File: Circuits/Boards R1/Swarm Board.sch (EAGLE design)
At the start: 89 parts, among them CON1 ISP(2X3), T1 NPN2N2222, T10 TEFT4300, T13 NPN2N2222, T14 NPN2N2222, T15 NPN2N2222, T16 NPN2N2222, T17 NPN2N2222, T18 NPN2N2222, T2 NPN2N2222, T3 NPN2N2222, T4 TEFT4300, T5 TEFT4300, T6 TEFT4300, T7 TEFT4300, T8 TEFT4300, T9 TEFT4300, U1 ATMEGA324P, U2 MCP73832SOT-23, U3 TB6552FN/FNG

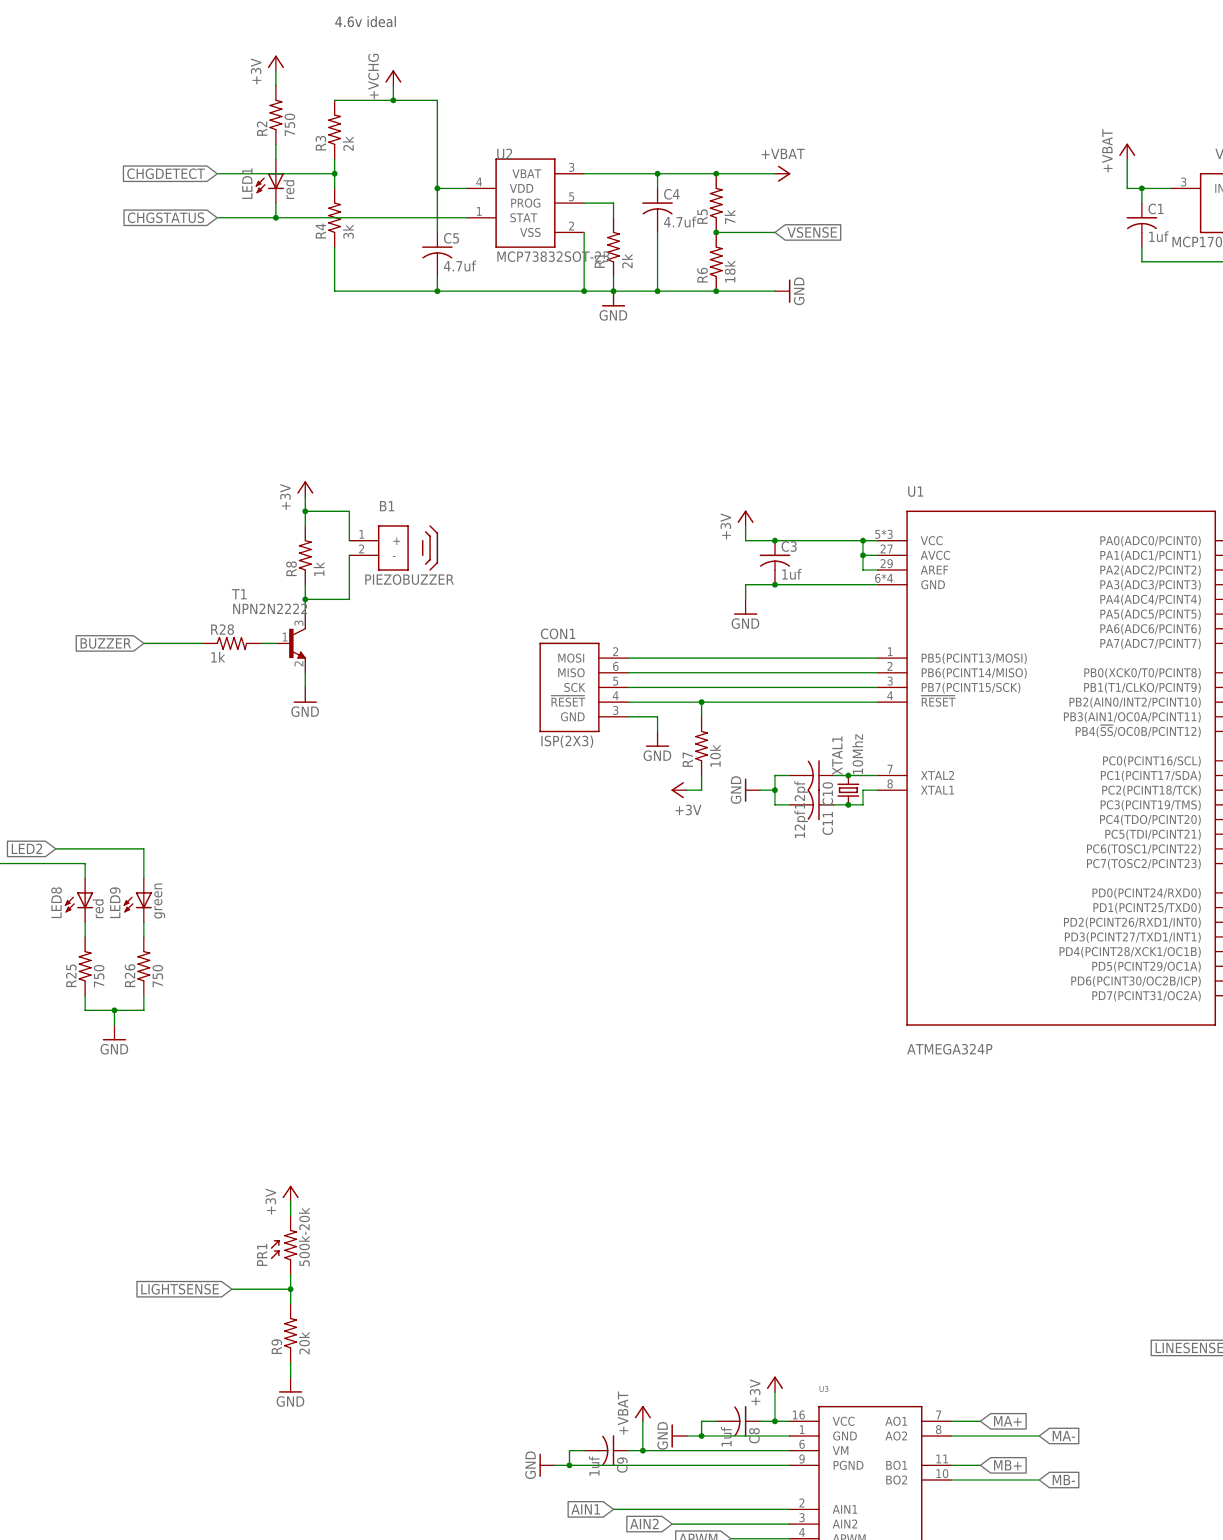
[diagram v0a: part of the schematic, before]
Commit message: 
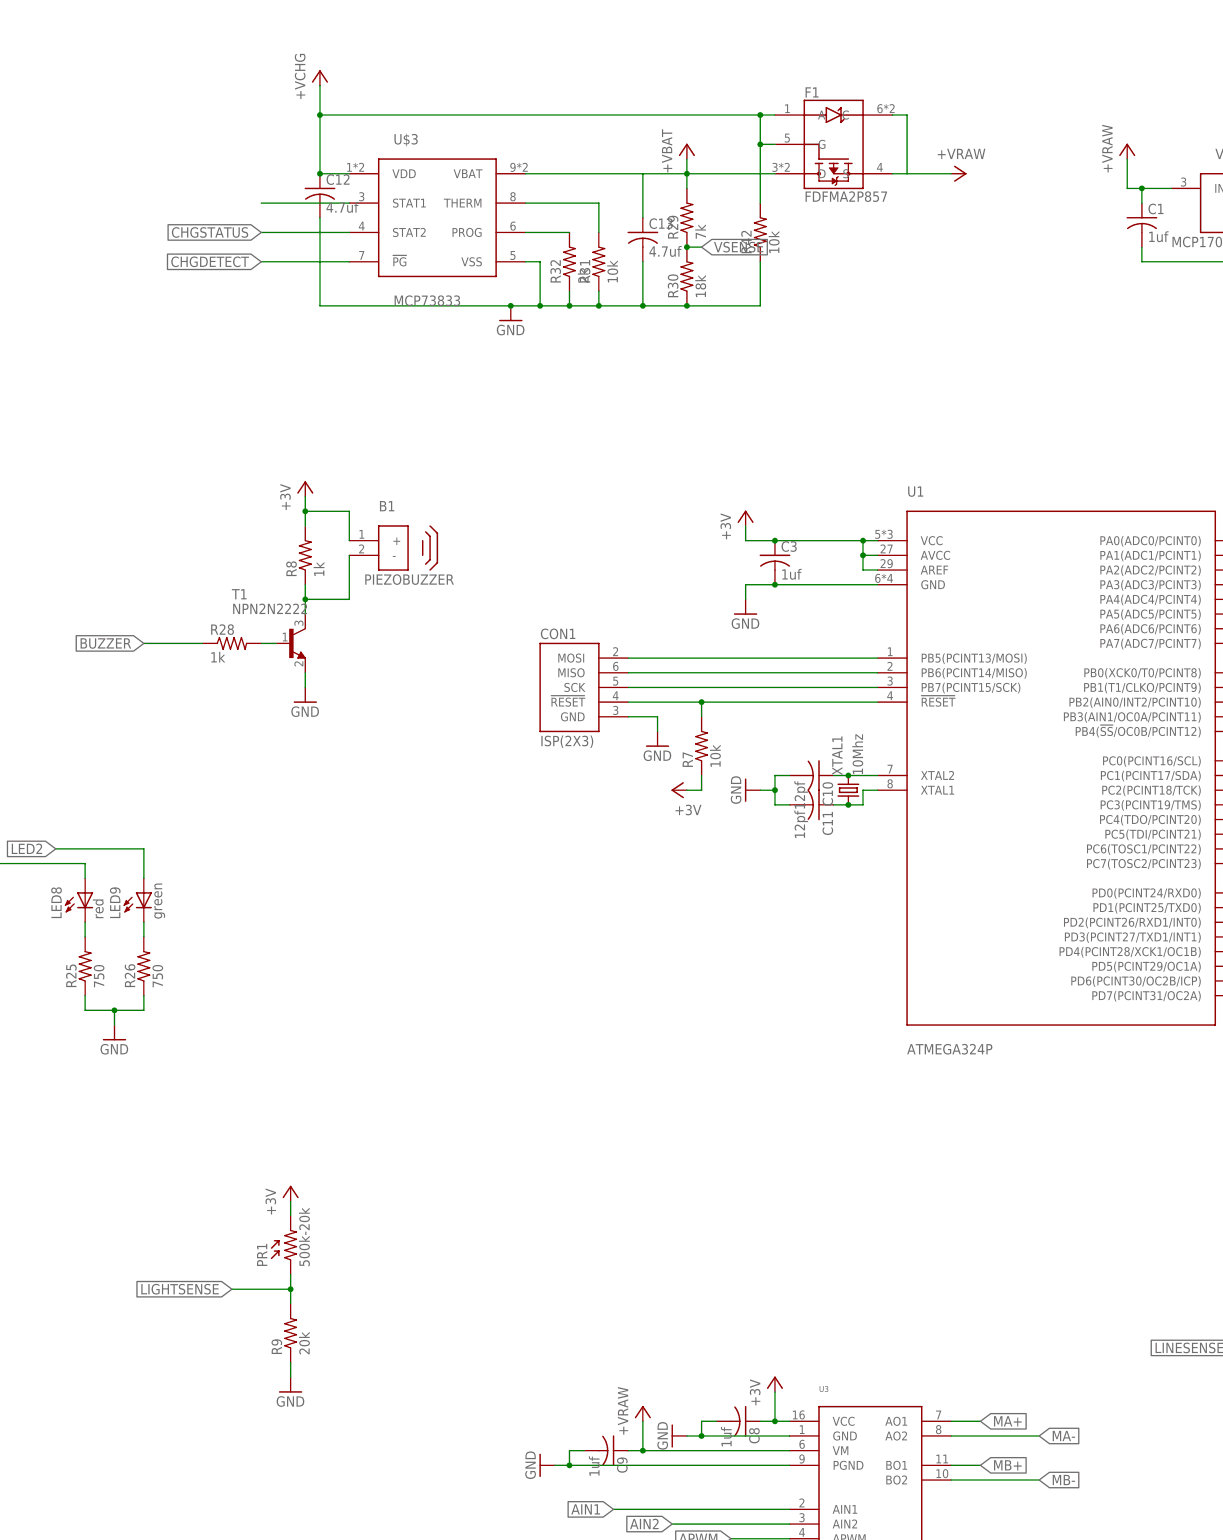
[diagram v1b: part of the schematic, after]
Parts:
- removed C4, C5: 4.7uf, Passive:CAP0603
- removed LED1: red, Passive:LED0603
- removed R1, R3: 2k, Passive:RES0603
- removed R2: 750, Passive:RES0603
- removed R4: 3k, Passive:RES0603
- removed R5: 7k, Passive:RES0603
- removed R6: 18k, Passive:RES0603
- removed U2: MCP73832SOT-23, PowerIC:MCP73832SOT-23
- added C12, C13: 4.7uf, Passive:CAP0603
- added F1: FDFMA2P857, Passive:FDFMA2P857
- added R29: 7k, Passive:RES0603
- added R30: 18k, Passive:RES0603
- added R31, R42: 10k, Passive:RES0603
- added R32: 2k, Passive:RES0603
- added U$3: MCP73833, PowerIC:MCP73833
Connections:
- removed net N$1: R1.2, U2.PROG
- removed net N$4: LED1.A, R2.1
- new net +VRAW: C1.1, C9.1, F1.C, F1.S, U3.VM, V1.IN
- new net N$22: R31.2, U$3.THERM
- new net N$28: R32.2, U$3.PROG
- new net N$31: U$3.VBAT
- new net N$33: U$3.STAT1
- net +3V: no longer R2.2
- net +VBAT: now also C13.1, F1.D, R29.2; no longer C1.1, C4.1, C9.1, R5.2, U2.VBAT, U3.VM, V1.IN
- net +VCHG: now also C12.1, F1.A, F1.G, R42.2, U$3.VDD; no longer C5.1, R3.2, U2.VDD
- net CHGDETECT: now also U$3.!PG; no longer R3.1, R4.2
- net CHGSTATUS: now also U$3.STAT2; no longer LED1.C, U2.STAT
- net GND: now also C12.2, C13.2, R30.1, R31.1, R32.1, R42.1, U$3.VSS; no longer C4.2, C5.2, R1.1, R4.1, R6.1, U2.VSS
- net VSENSE: now also R29.1, R30.2; no longer R5.1, R6.2
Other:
- note removed: "4.6v ideal"

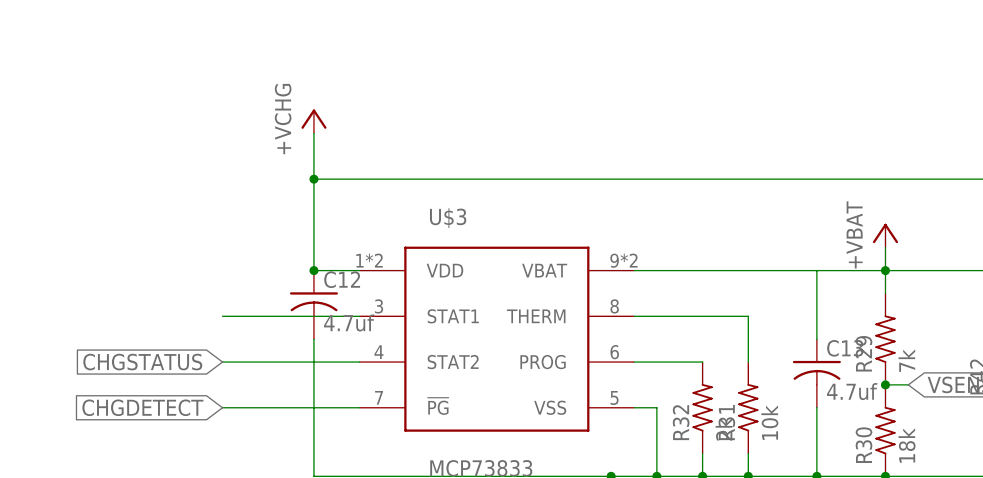
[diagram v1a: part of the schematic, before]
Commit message: changed charge circuit to incorporate mcp73833 and p-fet/diode for ppm
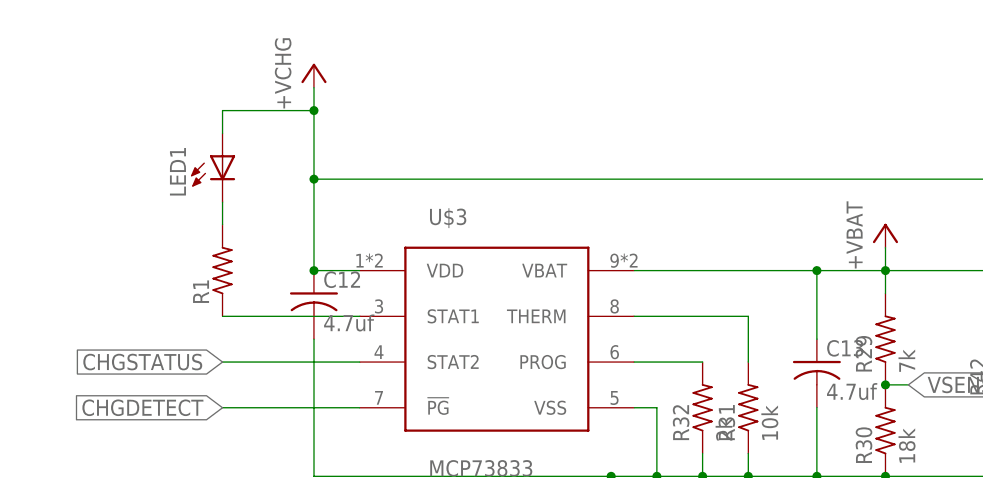
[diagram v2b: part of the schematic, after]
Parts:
- added LED1: (no value), Passive:LED0603
- added R1: (no value), Passive:RES0603
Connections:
- removed net N$31: U$3.VBAT
- new net N$1: LED1.C, R1.2
- net +VBAT: now also U$3.VBAT
- net +VCHG: now also LED1.A
- net N$33: now also R1.1
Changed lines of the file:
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@@
 <part name="P+2" library="Supply" deviceset="+VRAW" device=""/>
 <part name="P+13" library="Supply" deviceset="+VRAW" device=""/>
+<part name="LED1" library="Passive" deviceset="LED" device="0603"/>
+<part name="R1" library="Passive" deviceset="RES" device="0603"/>
 </parts>
 <sheets>
@@
 <instance part="R31" gate="G$1" x="-81.28" y="86.36" rot="R90"/>
 <instance part="R32" gate="G$1" x="-86.36" y="86.36" rot="R90"/>
-<instance part="P+14" gate="G$1" x="-129.54" y="116.84"/>
+<instance part="P+14" gate="G$1" x="-129.54" y="121.92"/>
 <instance part="P+18" gate="G$1" x="-66.04" y="104.14"/>
 <instance part="C12" gate="G$1" x="-129.54" y="96.52"/>
@@
 <instance part="P+2" gate="G$1" x="10.16" y="104.14"/>
 <instance part="P+13" gate="G$1" x="-73.66" y="-114.3"/>
+<instance part="LED1" gate="G$1" x="-139.7" y="114.3"/>
+<instance part="R1" gate="G$1" x="-139.7" y="101.6" rot="R90"/>
 </instances>
 <busses>
@@
 <wire x1="-66.04" y1="101.6" x2="-50.8" y2="101.6" width="0.1524" layer="91"/>
 <junction x="-66.04" y="101.6"/>
+<pinref part="U$3" gate="G$1" pin="VBAT"/>
+<wire x1="-93.98" y1="101.6" x2="-73.66" y2="101.6" width="0.1524" layer="91"/>
+<junction x="-73.66" y="101.6"/>
 </segment>
 </net>
@@
 <junction x="-129.54" y="101.6"/>
 <pinref part="F1" gate="G$1" pin="A"/>
-<wire x1="-129.54" y1="111.76" x2="-129.54" y2="116.84" width="0.1524" layer="91"/>
+<wire x1="-129.54" y1="111.76" x2="-129.54" y2="119.38" width="0.1524" layer="91"/>
+<wire x1="-129.54" y1="119.38" x2="-129.54" y2="121.92" width="0.1524" layer="91"/>
 <wire x1="-50.8" y1="111.76" x2="-53.34" y2="111.76" width="0.1524" layer="91"/>
 <pinref part="F1" gate="G$1" pin="G"/>
@@
 <junction x="-53.34" y="111.76"/>
 <junction x="-129.54" y="111.76"/>
+<pinref part="LED1" gate="G$1" pin="A"/>
+<wire x1="-129.54" y1="119.38" x2="-139.7" y2="119.38" width="0.1524" layer="91"/>
+<wire x1="-139.7" y1="119.38" x2="-139.7" y2="116.84" width="0.1524" layer="91"/>
+<junction x="-129.54" y="119.38"/>
 </segment>
 </net>
@@
 <pinref part="U$3" gate="G$1" pin="STAT1"/>
 <wire x1="-124.46" y1="96.52" x2="-139.7" y2="96.52" width="0.1524" layer="91"/>
+<pinref part="R1" gate="G$1" pin="1"/>
 </segment>
 </net>
@@
 <wire x1="-93.98" y1="96.52" x2="-81.28" y2="96.52" width="0.1524" layer="91"/>
 <wire x1="-81.28" y1="96.52" x2="-81.28" y2="91.44" width="0.1524" layer="91"/>
-</segment>
-</net>
-<net name="N$31" class="0">
-<segment>
-<pinref part="U$3" gate="G$1" pin="VBAT"/>
-<wire x1="-93.98" y1="101.6" x2="-73.66" y2="101.6" width="0.1524" layer="91"/>
 </segment>
 </net>
@@
 </segment>
 </net>
+<net name="N$1" class="0">
+<segment>
+<pinref part="R1" gate="G$1" pin="2"/>
+<pinref part="LED1" gate="G$1" pin="C"/>
+<wire x1="-139.7" y1="109.22" x2="-139.7" y2="106.68" width="0.1524" layer="91"/>
+</segment>
+</net>

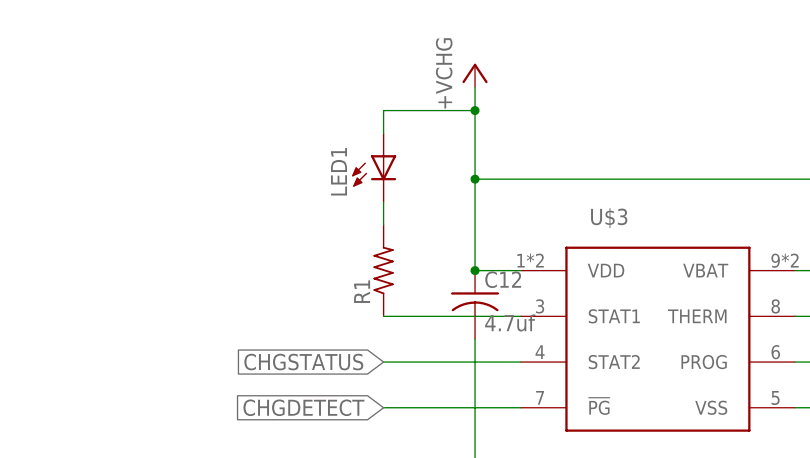
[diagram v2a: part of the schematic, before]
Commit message: 
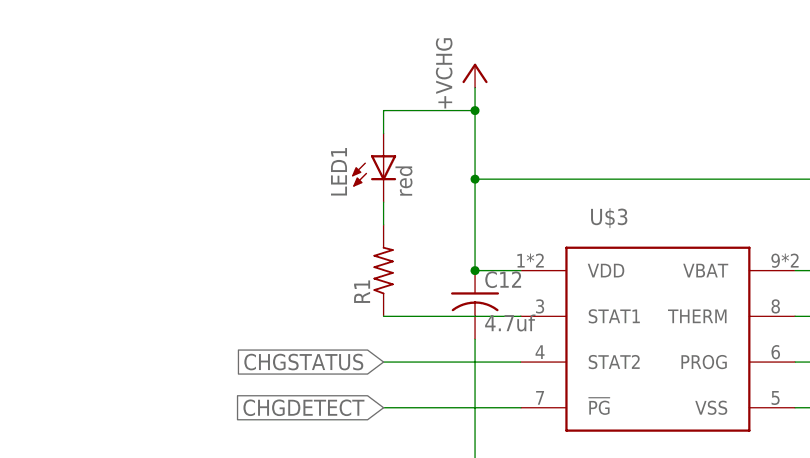
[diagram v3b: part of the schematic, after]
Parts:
- LED1: value (none) -> red
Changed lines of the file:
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@@
 <part name="P+2" library="Supply" deviceset="+VRAW" device=""/>
 <part name="P+13" library="Supply" deviceset="+VRAW" device=""/>
-<part name="LED1" library="Passive" deviceset="LED" device="0603"/>
+<part name="LED1" library="Passive" deviceset="LED" device="0603" value="red"/>
 <part name="R1" library="Passive" deviceset="RES" device="0603"/>
 </parts>
